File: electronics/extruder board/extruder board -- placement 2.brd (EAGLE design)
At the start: 35 x 51.2 mm, 22 parts, among them IC1 MAX6675, IC2 MAX6675, J1 Main THERMO, J2 AUX THERMO, J3 Main Heater, J4 Secondary HEATER, X1 22-23-2041, X2 Right Fan, X3 Left Fan, X4 Extruder Fan

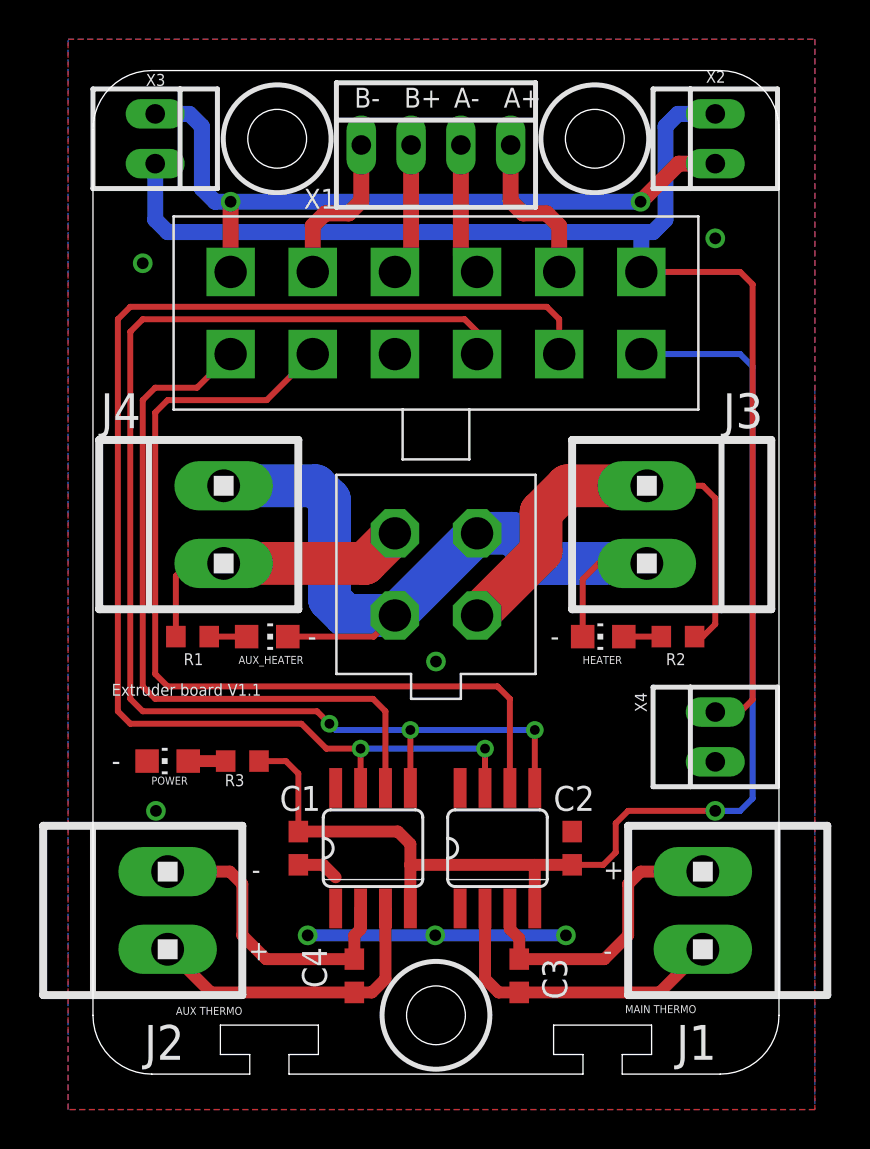
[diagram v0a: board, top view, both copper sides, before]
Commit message: Revert "Updated extruder board V1.1"
This reverts commit 2d423195ed33dd4a98d803fb0bad6f27ea0b4d36.
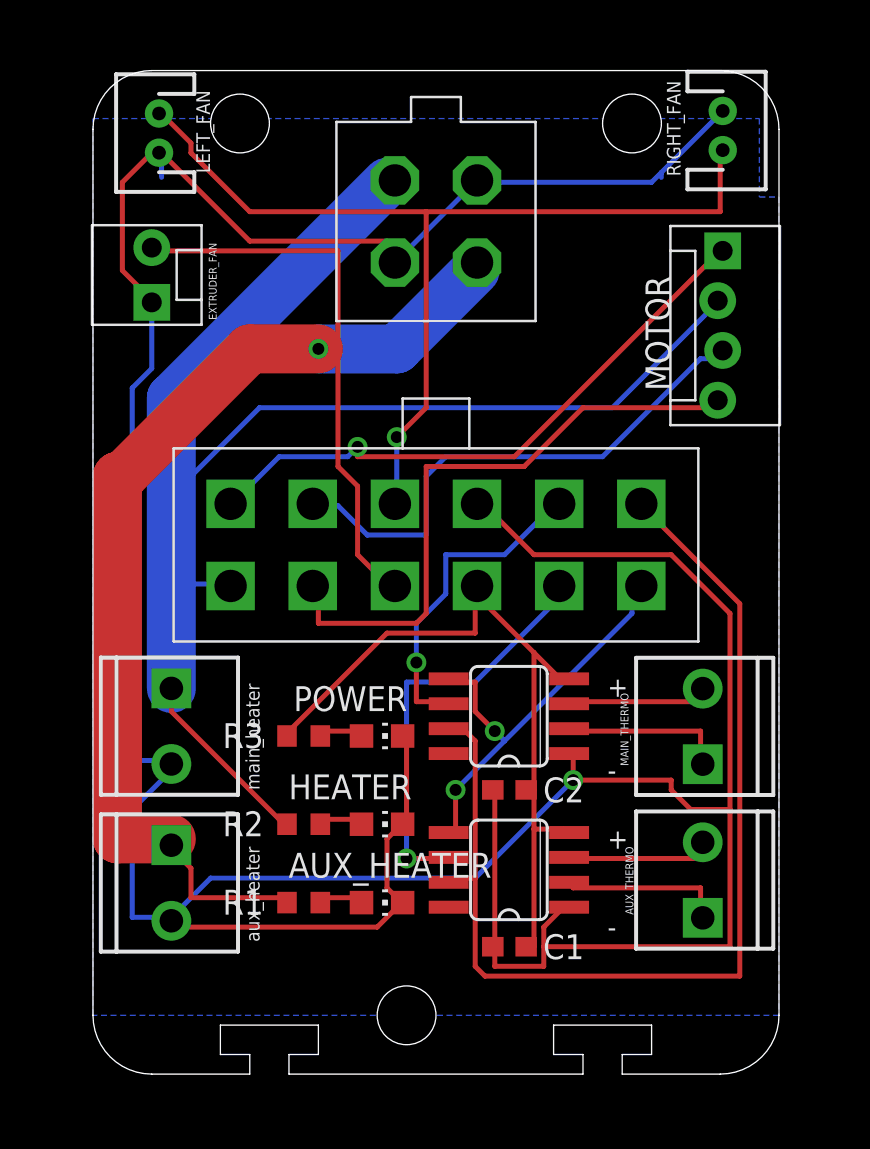
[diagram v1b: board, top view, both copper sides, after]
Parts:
- removed C3, C4: 0.1uF, rcl:C0603
- removed J1: Main THERMO, 555 delay toggle switch:CON-AMP_1X2MTA
- removed J2: AUX THERMO, 555 delay toggle switch:CON-AMP_1X2MTA
- removed J3: Main Heater, 555 delay toggle switch:CON-AMP_1X2MTA
- removed J4: Secondary HEATER, 555 delay toggle switch:CON-AMP_1X2MTA
- removed X1: 22-23-2041, con-molex:22-23-2041
- removed X2: Right Fan, con-molex:22-23-2021
- removed X3: Left Fan, con-molex:22-23-2021
- removed X4: Extruder Fan, con-molex:22-23-2021
- added AUX_THERMO, MAIN_HEATER, MAIN_THERMO, SECOND_HEATER: M023.5MM_LOCK, SparkFun-Connectors:SCREWTERMINAL-3.5MM-2_LOCK
- added EXTRUDER_FAN: M02POLAR_LOCK, extruder board -- placement 2:MOLEX-1X2_LOCK
- added LEFT_FAN, RIGHT_FAN: M02JST-PTH-2, extruder board -- placement 2:JST-2-PTH
- added MOTOR: (no value), extruder board -- placement 2:MOLEX-1X4_LOCK
- AUX_HEATER: value AUX HEATER -> (none)
- C1, C2: value 0.1uF -> (none)
- HEATER: value HEATER -> (none)
- POWER: value POWER -> (none)
- R1, R2, R3: value 1K -> (none)
- moved R2 21.4 mm to (10.8, 10.8), turned to 0 degrees
- moved U$3 18.0 mm to (17.5, 41.5), turned to 0 degrees
- moved HEATER 14.8 mm to (14.8, 10.8), turned to 270 degrees
- moved AUX_HEATER 14.8 mm to (14.8, 6.75)
- moved R1 14.7 mm to (10.8, 6.75)
- moved C1 11.9 mm to (21.2, 4.50), turned to 180 degrees
- moved U$1 11.8 mm to (17.5, 25.0), turned to 0 degrees
- moved POWER 11.0 mm to (14.8, 15.2), turned to 270 degrees
- moved IC2 7.02 mm to (21.2, 8.42), turned to 90 degrees
- moved IC1 6.76 mm to (21.2, 16.3), turned to 90 degrees
- moved C2 4.37 mm to (21.2, 12.5), turned to 180 degrees
- moved R3 3.38 mm to (10.8, 15.2), turned to 0 degrees
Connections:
- removed net HEATER_GND: AUX_HEATER.C, HEATER.C, J3.1, J4.1, U$3.2, U$3.3
- net +12V: now also EXTRUDER_FAN.2, U$1.6; no longer U$1.2, X2.2, X3.2, X4.2
- net AUX_HEATER: now also SECOND_HEATER.1; no longer J4.2
- net COOLING_FANS: now also LEFT_FAN.2, RIGHT_FAN.2, U$1.5; no longer U$1.12, X2.1, X3.1
- net CS2!: now also U$1.10; no longer U$1.11
- net DO: now also U$1.11; no longer U$1.3
- net GND: now also AUX_HEATER.C, EXTRUDER_FAN.1, HEATER.C, LEFT_FAN.1, MAIN_HEATER.2, RIGHT_FAN.1, SECOND_HEATER.2, U$3.2, U$3.3; no longer X4.1
- net HEATER: now also MAIN_HEATER.1; no longer J3.2
- net MOTOR_A+: now also MOTOR.1, U$1.1; no longer U$1.4, X1.4
- net MOTOR_A-: now also MOTOR.2, U$1.2; no longer U$1.6, X1.3
- net MOTOR_B+: now also MOTOR.3, U$1.3; no longer U$1.8, X1.2
- net MOTOR_B-: now also MOTOR.4, U$1.4; no longer U$1.10, X1.1
- net N$1: now also IC1.3, MAIN_THERMO.2; no longer C4.1, IC2.2, J2.1
- net N$2: now also MAIN_THERMO.1; no longer C3.1, J1.1
- net N$3: now also AUX_THERMO.2, IC2.3; no longer C3.2, IC1.3, J1.2
- net N$4: now also AUX_THERMO.1, IC2.2; no longer C4.2, IC2.3, J2.2
- net SCK: now also U$1.12; no longer U$1.5
- net VCC: now also U$1.8; no longer U$1.1
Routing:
- net GND: track 15.3 -> 195.9 mm, vias 7 -> 1
- net SCK: track 65.3 -> 21.8 mm, vias 3 -> 2
- net HEATER_GND: track 42.1 -> 0.00 mm
- net +12V: track 68.3 -> 28.1 mm
- net AUX_HEATER: track 15.2 -> 52.7 mm, vias 0 -> 1
- net MOTOR_A-: track 6.82 -> 38.9 mm
- net CS1!: track 45.8 -> 16.6 mm, vias 0 -> 1
- net VCC: track 64.4 -> 39.2 mm, vias 1 -> 0
- net MOTOR_B-: track 8.21 -> 31.5 mm
- net MOTOR_A+: track 8.21 -> 31.1 mm, vias 0 -> 1
- net MOTOR_B+: track 6.82 -> 27.3 mm
- net HEATER: track 24.1 -> 40.2 mm
- net CS2!: track 36.9 -> 21.5 mm, vias 0 -> 1
- net DO: track 68.4 -> 54.4 mm, vias 2 -> 0
- net COOLING_FANS: track 36.7 -> 49.7 mm, vias 2 -> 1
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- added copper zone on layer 16, net N$6
- removed copper zone on layer 1, net GND
- removed copper zone on layer 16, net GND
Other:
- board text added: "aux_heater"
- board text added: "main_heater"
- board text removed: "+12V"
- board text removed: "A+"
- board text removed: "A-"
- board text removed: "AUX THERMO"
- board text removed: "B+"
- board text removed: "B-"
- board text removed: "CS1"
- board text removed: "CS2"
- board text removed: "DO"
- board text removed: "Extruder board V1.1"
- board text removed: "FAN"
- board text removed: "GND"
- board text removed: "MAIN THERMO"
- board text removed: "SCK"
- board text removed: "VCC"

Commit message: extruder board rev1
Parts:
- removed AUX_THERMO, MAIN_HEATER, MAIN_THERMO, SECOND_HEATER: M023.5MM_LOCK, SparkFun-Connectors:SCREWTERMINAL-3.5MM-2_LOCK
- removed EXTRUDER_FAN: M02POLAR_LOCK, extruder board -- placement 2:MOLEX-1X2_LOCK
- removed LEFT_FAN, RIGHT_FAN: M02JST-PTH-2, extruder board -- placement 2:JST-2-PTH
- removed MOTOR: (no value), extruder board -- placement 2:MOLEX-1X4_LOCK
- added C3, C4: 0.1uF, rcl:C0603
- added J1: Main THERMO, 555 delay toggle switch:CON-AMP_1X2MTA
- added J2: AUX THERMO, 555 delay toggle switch:CON-AMP_1X2MTA
- added J3: Main Heater, 555 delay toggle switch:CON-AMP_1X2MTA
- added J4: Secondary HEATER, 555 delay toggle switch:CON-AMP_1X2MTA
- added X1: 22-23-2041, con-molex:22-23-2041
- added X2: Right Fan, con-molex:22-23-2021
- added X3: Left Fan, con-molex:22-23-2021
- added X4: Extruder Fan, con-molex:22-23-2021
- AUX_HEATER: value (none) -> AUX HEATER
- C1, C2: value (none) -> 0.1uF
- HEATER: value (none) -> HEATER
- POWER: value (none) -> POWER
- R1, R2, R3: value (none) -> 1K
- moved R2 21.4 mm to (29.8, 20.3), turned to 180 degrees
- moved U$3 18.0 mm to (17.5, 23.5), turned to 180 degrees
- moved HEATER 14.8 mm to (26.0, 20.3), turned to 90 degrees
- moved AUX_HEATER 14.8 mm to (8.89, 20.3)
- moved R1 14.7 mm to (5.08, 20.3)
- moved C1 11.9 mm to (10.5, 9.53), turned to 270 degrees
- moved U$1 11.8 mm to (17.5, 36.8), turned to 180 degrees
- moved POWER 11.8 mm to (3.05, 13.9), turned to 90 degrees
- moved IC2 7.02 mm to (14.3, 9.53), turned to 0 degrees
- moved IC1 6.76 mm to (20.6, 9.53), turned to 0 degrees
- moved C2 4.37 mm to (24.4, 9.53), turned to 90 degrees
- moved R3 3.88 mm to (7.11, 13.9), turned to 180 degrees
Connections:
- new net HEATER_GND: AUX_HEATER.C, HEATER.C, J3.1, J4.1, U$3.2, U$3.3
- net +12V: now also X4.2; no longer EXTRUDER_FAN.2
- net AUX_HEATER: now also J4.2; no longer SECOND_HEATER.1
- net COOLING_FANS: now also X2.2, X3.2; no longer LEFT_FAN.2, RIGHT_FAN.2
- net GND: now also X2.1, X3.1, X4.1; no longer AUX_HEATER.C, EXTRUDER_FAN.1, HEATER.C, LEFT_FAN.1, MAIN_HEATER.2, RIGHT_FAN.1, SECOND_HEATER.2, U$3.2, U$3.3
- net HEATER: now also J3.2; no longer MAIN_HEATER.1
- net MOTOR_A+: now also X1.4; no longer MOTOR.1
- net MOTOR_A-: now also X1.3; no longer MOTOR.2
- net MOTOR_B+: now also X1.2; no longer MOTOR.3
- net MOTOR_B-: now also X1.1; no longer MOTOR.4
- net N$1: now also C4.1, IC2.2, J2.1; no longer IC1.3, MAIN_THERMO.2
- net N$2: now also C3.1, J1.1; no longer MAIN_THERMO.1
- net N$3: now also C3.2, IC1.3, J1.2; no longer AUX_THERMO.2, IC2.3
- net N$4: now also C4.2, IC2.3, J2.2; no longer AUX_THERMO.1, IC2.2
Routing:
- net GND: track 195.9 -> 15.3 mm, vias 1 -> 5
- net HEATER_GND: track 0.00 -> 42.1 mm
- net AUX_HEATER: track 52.7 -> 15.2 mm, vias 1 -> 0
- net VCC: track 39.2 -> 71.9 mm, vias 0 -> 1
- net SCK: track 21.8 -> 54.2 mm, vias 2 -> 3
- net CS1!: track 16.6 -> 47.7 mm
- net MOTOR_A-: track 38.9 -> 14.9 mm
- net CS2!: track 21.5 -> 42.8 mm, vias 1 -> 0
- net HEATER: track 40.2 -> 24.1 mm
- net MOTOR_B-: track 31.5 -> 15.7 mm
- net MOTOR_A+: track 31.1 -> 16.2 mm, vias 1 -> 0
- net MOTOR_B+: track 27.3 -> 17.1 mm
- net +12V: track 28.1 -> 37.7 mm
- net N$1: track 7.43 -> 15.6 mm
- net N$3: track 7.56 -> 15.5 mm
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- added copper zone on layer 1, net GND
- added copper zone on layer 16, net GND
- removed copper zone on layer 16, net N$6
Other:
- board text added: "A+"
- board text added: "A-"
- board text added: "AUX THERMO"
- board text added: "B+"
- board text added: "B-"
- board text added: "MAIN THERMO"
- board text removed: "aux_heater"
- board text removed: "main_heater"
